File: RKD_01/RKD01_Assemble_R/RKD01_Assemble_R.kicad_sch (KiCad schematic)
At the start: 86 parts, among them J2 TRRS, SW31 SW_Push, SW32 SW_Push, SW33 SW_Push, SW34 SW_Push, SW35 SW_Push, SW36 SW_Push, SW37 SW_Push, SW38 SW_Push, SW39 SW_Push, SW40 SW_Push, SW41 SW_Push, SW42 SW_Push, SW43 SW_Push, SW44 SW_Push, SW45 SW_Push, SW46 SW_Push, SW47 SW_Push, SW48 SW_Push, SW49 SW_Push, SW50 SW_Push, SW51 SW_Push, SW52 SW_Push, SW53 SW_Push, SW54 SW_Push, SW55 SW_Push, SW56 SW_Push, SW57 SW_Push, SW58 SW_Push, SW59 SW_Push, SW60 SW_Push, SW61 SW_Push, SW62 SW_Push, SW63 SW_Push, SW64 SW_Push, SW65 SW_Push, SW66 SW_Push, SW67 SW_Push, SW68 SW_Push, SW69 SW_Push, SW70 SW_Push, SW71 SW_Push, SW72 SW_Push, U2 ProMicro

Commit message: 右手 OLED追加、SW番号調整
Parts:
- added OL2: OLED, symbol BrownSugar_KBD:OLED
- renumbered D31 to D36, D32 to D37, D33 to D38, D34 to D39, D35 to D40, D36 to D41, D37 to D42, D38 to D43, D39 to D44, D40 to D45, D41 to D46, D42 to D47, D43 to D48, D44 to D49, D45 to D50, D46 to D51, D47 to D52, D48 to D53, D49 to D54, D50 to D55, D51 to D56, D52 to D57, D53 to D58, D54 to D59, D55 to D60, D56 to D61, D57 to D62, D58 to D63, D59 to D64, D60 to D65, D61 to D66, D62 to D67, D63 to D68, D64 to D69, D65 to D70, D66 to D71, D67 to D72, D68 to D73, D69 to D74, D70 to D75, D71 to D76, SW31 to SW36, SW32 to SW37, SW33 to SW38, SW34 to SW39, SW35 to SW40, SW36 to SW41, SW37 to SW42, SW38 to SW43, SW39 to SW44, SW40 to SW45, SW41 to SW46, SW42 to SW47, SW43 to SW48, SW44 to SW49, SW45 to SW50, SW46 to SW51, SW47 to SW52, SW48 to SW53, SW49 to SW54, SW50 to SW55, SW51 to SW56, SW52 to SW57, SW53 to SW58, SW54 to SW59, SW55 to SW60, SW56 to SW61, SW57 to SW62, SW58 to SW63, SW59 to SW64, SW60 to SW65, SW61 to SW66, SW62 to SW67, SW63 to SW68, SW64 to SW69, SW65 to SW70, SW66 to SW71, SW67 to SW72, SW68 to SW73, SW69 to SW74, SW70 to SW75, SW71 to SW76, SW72 to SW77
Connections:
- net Col7: now also U2.13 (10/B6); no longer U2.11 (B4/8)
- net GND: now also U2.2 (D2/RX1), OL2.4 (GND); no longer U2.13 (10/B6)
- net Row0: now also U2.7 (D4/4); no longer U2.2 (D2/RX1)
- net Row1: now also U2.8 (C6/5); no longer U2.7 (D4/4)
- net Row2: now also U2.9 (D7/6); no longer U2.8 (C6/5)
- net Row3: now also U2.10 (E6/7); no longer U2.9 (D7/6)
- net Row4: now also U2.11 (B4/8); no longer U2.10 (E6/7)
- net SCL: now also OL2.2 (SCL)
- net SDA: now also OL2.1 (SDA)
- net VCC: now also OL2.3 (VCC)
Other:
- moved on the sheet: Trackball1

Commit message: 配線実施
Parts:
- D36, D37, D38, D39, D40, D41, D42, D43, D44, D45, D46, D47, D48, D49, D50, D51, D52, D53, D54, D55, D56, D57, D58, D59, D60, D61, D62, D63, D64, D65, D66, D67, D68, D69, D70, D71, D72, D73, D74, D75, D76: footprint (none) -> kbd_Parts:Diode_SMD
- J2: footprint (none) -> BrownSugar_KBD:TRRS_PJ-320A
- OL2: footprint (none) -> BrownSugar_KBD:OLED_center_module
- SW36, SW37, SW38, SW39, SW40, SW41, SW42, SW43, SW44, SW45, SW46, SW47, SW48, SW49, SW50, SW51, SW52, SW53, SW54, SW55, SW56, SW57, SW58, SW59, SW60, SW61, SW62, SW63, SW64, SW65, SW66, SW67, SW68, SW69, SW71, SW72, SW74, SW75, SW76: footprint (none) -> kbd_SW:Choc_Hotswap_1u
- SW70, SW73: footprint (none) -> kbd_SW:Choc_Hotswap_2u_Stab
- SW77: footprint (none) -> kbd_Parts:ResetSW
- Trackball1: footprint (none) -> kicad:AZ1UBALL
- U2: footprint (none) -> BrownSugar_KBD:ProMicro_r
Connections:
- net Col0: now also SW36.2, SW37.2, SW38.2, SW39.2; no longer SW36.1, SW37.1, SW38.1, SW39.1
- net Col1: now also SW40.2, SW41.2, SW42.2, SW43.2; no longer SW40.1, SW41.1, SW42.1, SW43.1
- net Col2: now also SW44.2, SW45.2, SW46.2, SW47.2, SW48.2; no longer SW44.1, SW45.1, SW46.1, SW47.1, SW48.1
- net Col3: now also SW49.2, SW50.2, SW51.2, SW52.2, SW53.2; no longer SW49.1, SW50.1, SW51.1, SW52.1, SW53.1
- net Col4: now also SW54.2, SW55.2, SW56.2, SW57.2; no longer SW54.1, SW55.1, SW56.1, SW57.1
- net Col5: now also SW58.2, SW59.2, SW60.2, SW61.2, SW62.2; no longer SW58.1, SW59.1, SW60.1, SW61.1, SW62.1
- net Col6: now also SW63.2, SW64.2, SW65.2, SW66.2, SW67.2; no longer SW63.1, SW64.1, SW65.1, SW66.1, SW67.1
- net Col7: now also SW68.2, SW69.2, SW70.2, SW71.2, SW72.2; no longer SW68.1, SW69.1, SW70.1, SW71.1, SW72.1
- net Col8: now also SW73.2, SW74.2, SW75.2, SW76.2; no longer SW73.1, SW74.1, SW75.1, SW76.1
- net at D45.2 (A): now also SW45.1; no longer SW45.2
- net at D75.2 (A): now also SW75.1; no longer SW75.2
- net at D59.2 (A): now also SW59.1; no longer SW59.2
- net at D48.2 (A): now also SW48.1; no longer SW48.2
- net at D52.2 (A): now also SW52.1; no longer SW52.2
- net at D68.2 (A): now also SW68.1; no longer SW68.2
- net at D39.2 (A): now also SW39.1; no longer SW39.2
- net at D73.2 (A): now also SW73.1; no longer SW73.2
- net at D46.2 (A): now also SW46.1; no longer SW46.2
- net at D53.2 (A): now also SW53.1; no longer SW53.2
- net at D66.2 (A): now also SW66.1; no longer SW66.2
- net at D70.2 (A): now also SW70.1; no longer SW70.2
- net at D69.2 (A): now also SW69.1; no longer SW69.2
- net at D72.2 (A): now also SW72.1; no longer SW72.2
- net at D55.2 (A): now also SW55.1; no longer SW55.2
- net at D64.2 (A): now also SW64.1; no longer SW64.2
- net at D65.2 (A): now also SW65.1; no longer SW65.2
- net at D60.2 (A): now also SW60.1; no longer SW60.2
- net at D47.2 (A): now also SW47.1; no longer SW47.2
- net at D49.2 (A): now also SW49.1; no longer SW49.2
- net at D58.2 (A): now also SW58.1; no longer SW58.2
- net at D41.2 (A): now also SW41.1; no longer SW41.2
- net at D50.2 (A): now also SW50.1; no longer SW50.2
- net at D38.2 (A): now also SW38.1; no longer SW38.2
- net at D62.2 (A): now also SW62.1; no longer SW62.2
- net at D61.2 (A): now also SW61.1; no longer SW61.2
- net at D54.2 (A): now also SW54.1; no longer SW54.2
- net at D74.2 (A): now also SW74.1; no longer SW74.2
- net at D37.2 (A): now also SW37.1; no longer SW37.2
- net at D43.2 (A): now also SW43.1; no longer SW43.2
- net at D40.2 (A): now also SW40.1; no longer SW40.2
- net at D44.2 (A): now also SW44.1; no longer SW44.2
- net at D71.2 (A): now also SW71.1; no longer SW71.2
- net at D67.2 (A): now also SW67.1; no longer SW67.2
- net at D76.2 (A): now also SW76.1; no longer SW76.2
- net at D63.2 (A): now also SW63.1; no longer SW63.2
- net at D42.2 (A): now also SW42.1; no longer SW42.2
- net at D57.2 (A): now also SW57.1; no longer SW57.2
- net at D56.2 (A): now also SW56.1; no longer SW56.2
- net at D36.2 (A): now also SW36.1; no longer SW36.2
- net at D51.2 (A): now also SW51.1; no longer SW51.2

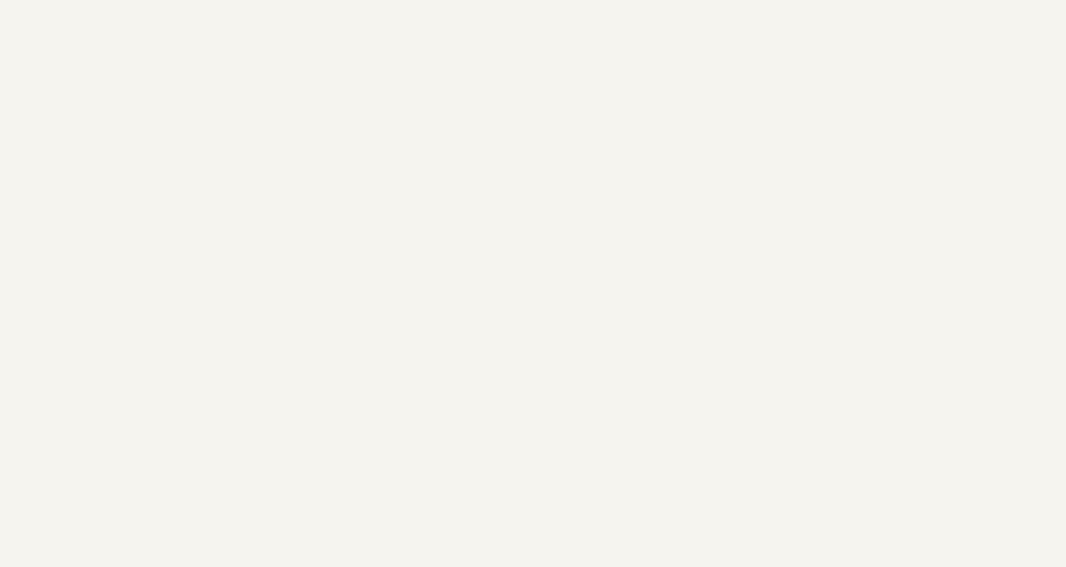
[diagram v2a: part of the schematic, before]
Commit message: 右手 自動配線用マーク追加
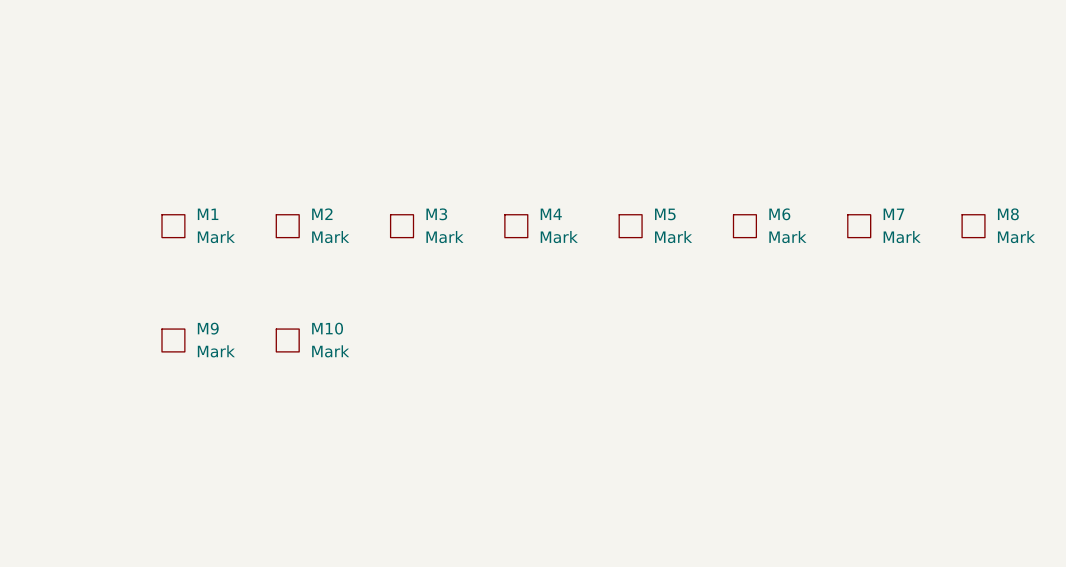
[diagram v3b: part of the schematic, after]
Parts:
- added M1, M2, M3, M4, M5, M6, M7, M8: Mark, kbd_Hole:m2_Spacer_Hole_hex, symbol BrownSugar_KBD:Mark
- added M10, M9: Mark, kbd_Hole:m2_Screw_Hole, symbol BrownSugar_KBD:Mark

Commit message: ダイオードを表面・貫通両対応
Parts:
- D36, D37, D38, D39, D40, D41, D42, D43, D44, D45, D46, D47, D48, D49, D50, D51, D52, D53, D54, D55, D56, D57, D58, D59, D60, D61, D62, D63, D64, D65, D66, D67, D68, D69, D70, D71, D72, D73, D74, D75, D76: footprint kbd_Parts:Diode_SMD -> kbd_Parts:Diode_TH_SMD
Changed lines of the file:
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@@
 			)
 		)
-		(property "Footprint" "kbd_Parts:Diode_SMD"
+		(property "Footprint" "kbd_Parts:Diode_TH_SMD"
 			(at 106.68 156.21 0)
 			(effects
@@
 			)
 		)
-		(property "Footprint" "kbd_Parts:Diode_SMD"
+		(property "Footprint" "kbd_Parts:Diode_TH_SMD"
 			(at 182.88 156.21 0)
 			(effects
@@
 			)
 		)
-		(property "Footprint" "kbd_Parts:Diode_SMD"
+		(property "Footprint" "kbd_Parts:Diode_TH_SMD"
 			(at 106.68 232.41 0)
 			(effects
@@
 			)
 		)
-		(property "Footprint" "kbd_Parts:Diode_SMD"
+		(property "Footprint" "kbd_Parts:Diode_TH_SMD"
 			(at 233.68 130.81 0)
 			(effects
@@
 			)
 		)
-		(property "Footprint" "kbd_Parts:Diode_SMD"
+		(property "Footprint" "kbd_Parts:Diode_TH_SMD"
 			(at 259.08 130.81 0)
 			(effects
@@
 			)
 		)
-		(property "Footprint" "kbd_Parts:Diode_SMD"
+		(property "Footprint" "kbd_Parts:Diode_TH_SMD"
 			(at 132.08 232.41 0)
 			(effects
@@
 			)
 		)
-		(property "Footprint" "kbd_Parts:Diode_SMD"
+		(property "Footprint" "kbd_Parts:Diode_TH_SMD"
 			(at 208.28 207.01 0)
 			(effects
@@
 			)
 		)
-		(property "Footprint" "kbd_Parts:Diode_SMD"
+		(property "Footprint" "kbd_Parts:Diode_TH_SMD"
 			(at 132.08 207.01 0)
 			(effects
@@
 			)
 		)
-		(property "Footprint" "kbd_Parts:Diode_SMD"
+		(property "Footprint" "kbd_Parts:Diode_TH_SMD"
 			(at 233.68 156.21 0)
 			(effects
@@
 			)
 		)
-		(property "Footprint" "kbd_Parts:Diode_SMD"
+		(property "Footprint" "kbd_Parts:Diode_TH_SMD"
 			(at 233.68 232.41 0)
 			(effects
@@
 			)
 		)
-		(property "Footprint" "kbd_Parts:Diode_SMD"
+		(property "Footprint" "kbd_Parts:Diode_TH_SMD"
 			(at 157.48 156.21 0)
 			(effects
@@
 			)
 		)
-		(property "Footprint" "kbd_Parts:Diode_SMD"
+		(property "Footprint" "kbd_Parts:Diode_TH_SMD"
 			(at 106.68 207.01 0)
 			(effects
@@
 			)
 		)
-		(property "Footprint" "kbd_Parts:Diode_SMD"
+		(property "Footprint" "kbd_Parts:Diode_TH_SMD"
 			(at 132.08 130.81 0)
 			(effects
@@
 			)
 		)
-		(property "Footprint" "kbd_Parts:Diode_SMD"
+		(property "Footprint" "kbd_Parts:Diode_TH_SMD"
 			(at 182.88 130.81 0)
 			(effects
@@
 			)
 		)
-		(property "Footprint" "kbd_Parts:Diode_SMD"
+		(property "Footprint" "kbd_Parts:Diode_TH_SMD"
 			(at 132.08 156.21 0)
 			(effects
@@
 			)
 		)
-		(property "Footprint" "kbd_Parts:Diode_SMD"
+		(property "Footprint" "kbd_Parts:Diode_TH_SMD"
 			(at 259.08 207.01 0)
 			(effects
@@
 			)
 		)
-		(property "Footprint" "kbd_Parts:Diode_SMD"
+		(property "Footprint" "kbd_Parts:Diode_TH_SMD"
 			(at 182.88 232.41 0)
 			(effects
@@
 			)
 		)
-		(property "Footprint" "kbd_Parts:Diode_SMD"
+		(property "Footprint" "kbd_Parts:Diode_TH_SMD"
 			(at 106.68 181.61 0)
 			(effects
@@
 			)
 		)
-		(property "Footprint" "kbd_Parts:Diode_SMD"
+		(property "Footprint" "kbd_Parts:Diode_TH_SMD"
 			(at 55.88 207.01 0)
 			(effects
@@
 			)
 		)
-		(property "Footprint" "kbd_Parts:Diode_SMD"
+		(property "Footprint" "kbd_Parts:Diode_TH_SMD"
 			(at 208.28 181.61 0)
 			(effects
@@
 			)
 		)
-		(property "Footprint" "kbd_Parts:Diode_SMD"
+		(property "Footprint" "kbd_Parts:Diode_TH_SMD"
 			(at 182.88 207.01 0)
 			(effects
@@
 			)
 		)
-		(property "Footprint" "kbd_Parts:Diode_SMD"
+		(property "Footprint" "kbd_Parts:Diode_TH_SMD"
 			(at 157.48 130.81 0)
 			(effects
@@
 			)
 		)
-		(property "Footprint" "kbd_Parts:Diode_SMD"
+		(property "Footprint" "kbd_Parts:Diode_TH_SMD"
 			(at 55.88 181.61 0)
 			(effects
@@
 			)
 		)
-		(property "Footprint" "kbd_Parts:Diode_SMD"
+		(property "Footprint" "kbd_Parts:Diode_TH_SMD"
 			(at 81.28 130.81 0)
 			(effects
@@
 			)
 		)
-		(property "Footprint" "kbd_Parts:Diode_SMD"
+		(property "Footprint" "kbd_Parts:Diode_TH_SMD"
 			(at 106.68 130.81 0)
 			(effects
@@
 			)
 		)
-		(property "Footprint" "kbd_Parts:Diode_SMD"
+		(property "Footprint" "kbd_Parts:Diode_TH_SMD"
 			(at 259.08 232.41 0)
 			(effects
@@
 			)
 		)
-		(property "Footprint" "kbd_Parts:Diode_SMD"
+		(property "Footprint" "kbd_Parts:Diode_TH_SMD"
 			(at 208.28 130.81 0)
 			(effects
@@
 			)
 		)
-		(property "Footprint" "kbd_Parts:Diode_SMD"
+		(property "Footprint" "kbd_Parts:Diode_TH_SMD"
 			(at 182.88 181.61 0)
 			(effects
@@
 			)
 		)
-		(property "Footprint" "kbd_Parts:Diode_SMD"
+		(property "Footprint" "kbd_Parts:Diode_TH_SMD"
 			(at 208.28 232.41 0)
 			(effects
@@
 			)
 		)
-		(property "Footprint" "kbd_Parts:Diode_SMD"
+		(property "Footprint" "kbd_Parts:Diode_TH_SMD"
 			(at 81.28 207.01 0)
 			(effects
@@
 			)
 		)
-		(property "Footprint" "kbd_Parts:Diode_SMD"
+		(property "Footprint" "kbd_Parts:Diode_TH_SMD"
 			(at 208.28 156.21 0)
 			(effects
@@
 			)
 		)
-		(property "Footprint" "kbd_Parts:Diode_SMD"
+		(property "Footprint" "kbd_Parts:Diode_TH_SMD"
 			(at 81.28 156.21 0)
 			(effects
@@
 			)
 		)
-		(property "Footprint" "kbd_Parts:Diode_SMD"
+		(property "Footprint" "kbd_Parts:Diode_TH_SMD"
 			(at 157.48 207.01 0)
 			(effects
@@
 			)
 		)
-		(property "Footprint" "kbd_Parts:Diode_SMD"
+		(property "Footprint" "kbd_Parts:Diode_TH_SMD"
 			(at 157.48 181.61 0)
 			(effects
@@
 			)
 		)
-		(property "Footprint" "kbd_Parts:Diode_SMD"
+		(property "Footprint" "kbd_Parts:Diode_TH_SMD"
 			(at 55.88 130.81 0)
 			(effects
@@
 			)
 		)
-		(property "Footprint" "kbd_Parts:Diode_SMD"
+		(property "Footprint" "kbd_Parts:Diode_TH_SMD"
 			(at 132.08 181.61 0)
 			(effects
@@
 			)
 		)
-		(property "Footprint" "kbd_Parts:Diode_SMD"
+		(property "Footprint" "kbd_Parts:Diode_TH_SMD"
 			(at 233.68 181.61 0)
 			(effects
@@
 			)
 		)
-		(property "Footprint" "kbd_Parts:Diode_SMD"
+		(property "Footprint" "kbd_Parts:Diode_TH_SMD"
 			(at 81.28 181.61 0)
 			(effects
@@
 			)
 		)
-		(property "Footprint" "kbd_Parts:Diode_SMD"
+		(property "Footprint" "kbd_Parts:Diode_TH_SMD"
 			(at 55.88 232.41 0)
 			(effects
@@
 			)
 		)
-		(property "Footprint" "kbd_Parts:Diode_SMD"
+		(property "Footprint" "kbd_Parts:Diode_TH_SMD"
 			(at 233.68 207.01 0)
 			(effects
@@
 			)
 		)
-		(property "Footprint" "kbd_Parts:Diode_SMD"
+		(property "Footprint" "kbd_Parts:Diode_TH_SMD"
 			(at 259.08 156.21 0)
 			(effects
